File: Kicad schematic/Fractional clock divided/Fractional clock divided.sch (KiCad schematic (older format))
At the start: 51 parts, among them Q1 2N3904, Q2 2N3904, Q3 2N3904, Q4 2N3904, SW1 SPDT on-on, SW2 SPDT on-off-on, SW3 SPDT on-on, SW4 Rotary_Encoder_Switch, U1 TL074, U2 Teensy-LC

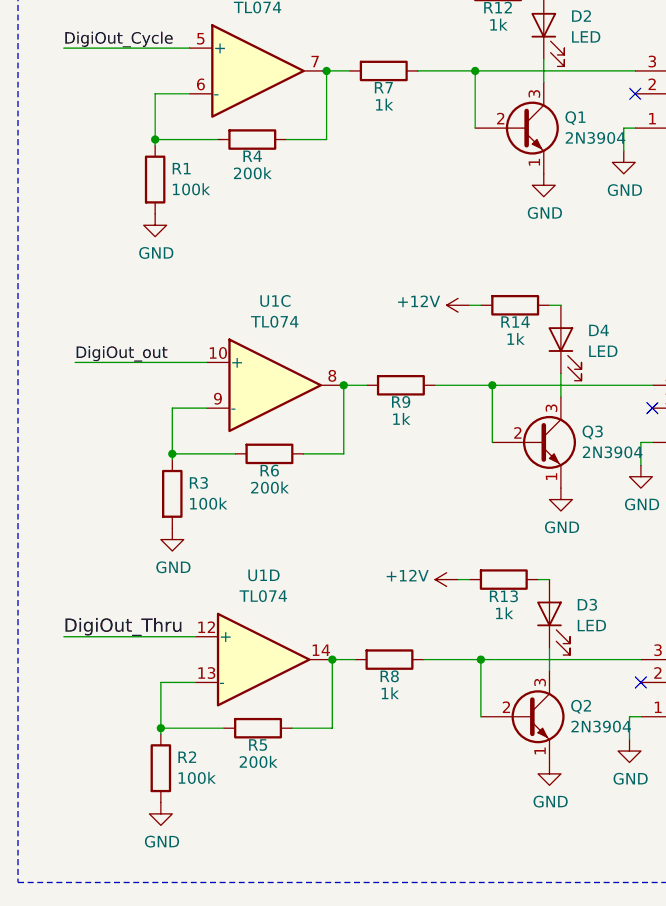
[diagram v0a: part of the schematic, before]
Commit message: Changed output voltages to 5V.
Changed all output voltages to 5V.
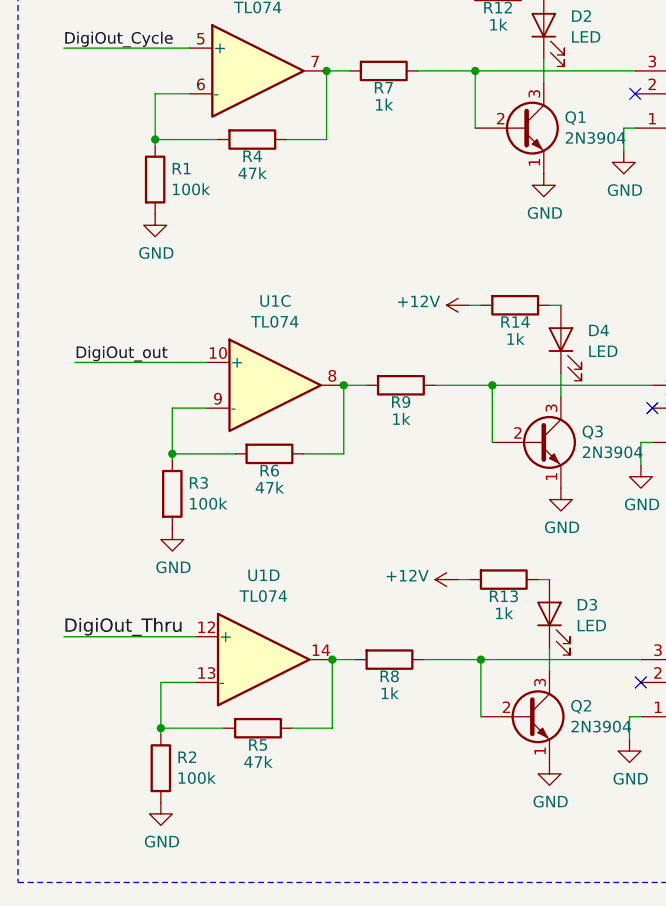
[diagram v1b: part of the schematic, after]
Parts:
- R4, R5, R6: value 200k -> 47k
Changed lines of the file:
@@
 EESchema Schematic File Version 4
+LIBS:Fractional clock divided-cache
 EELAYER 26 0
 EELAYER END
@@
 P 1725 3850
 F 0 "R4" V 1800 3850 50  0000 C CNN
-F 1 "200k" V 1875 3850 50  0000 C CNN
+F 1 "47k" V 1875 3850 50  0000 C CNN
 F 2 "" V 1655 3850 50  0001 C CNN
 F 3 "~" H 1725 3850 50  0001 C CNN
@@
 P 1800 5225
 F 0 "R6" V 1875 5225 50  0000 C CNN
-F 1 "200k" V 1950 5225 50  0000 C CNN
+F 1 "47k" V 1950 5225 50  0000 C CNN
 F 2 "" V 1730 5225 50  0001 C CNN
 F 3 "~" H 1800 5225 50  0001 C CNN
@@
 P 1750 6425
 F 0 "R5" V 1825 6425 50  0000 C CNN
-F 1 "200k" V 1900 6425 50  0000 C CNN
+F 1 "47k" V 1900 6425 50  0000 C CNN
 F 2 "" V 1680 6425 50  0001 C CNN
 F 3 "~" H 1750 6425 50  0001 C CNN

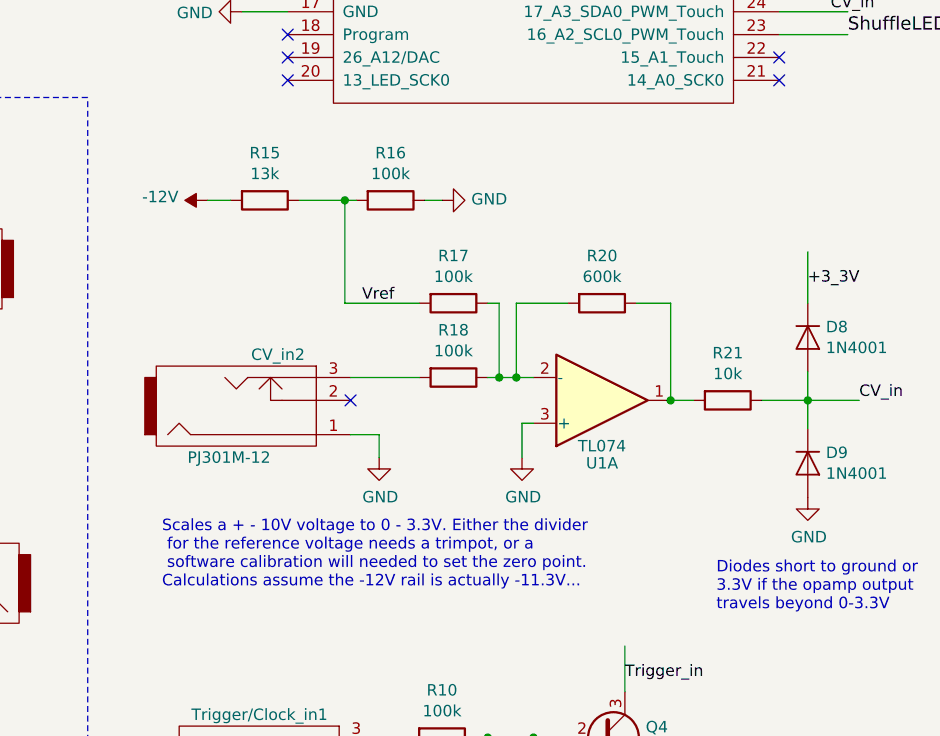
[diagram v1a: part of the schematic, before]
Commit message: Resistor substitution
Substituting resisitors to reflect what I have at-hand
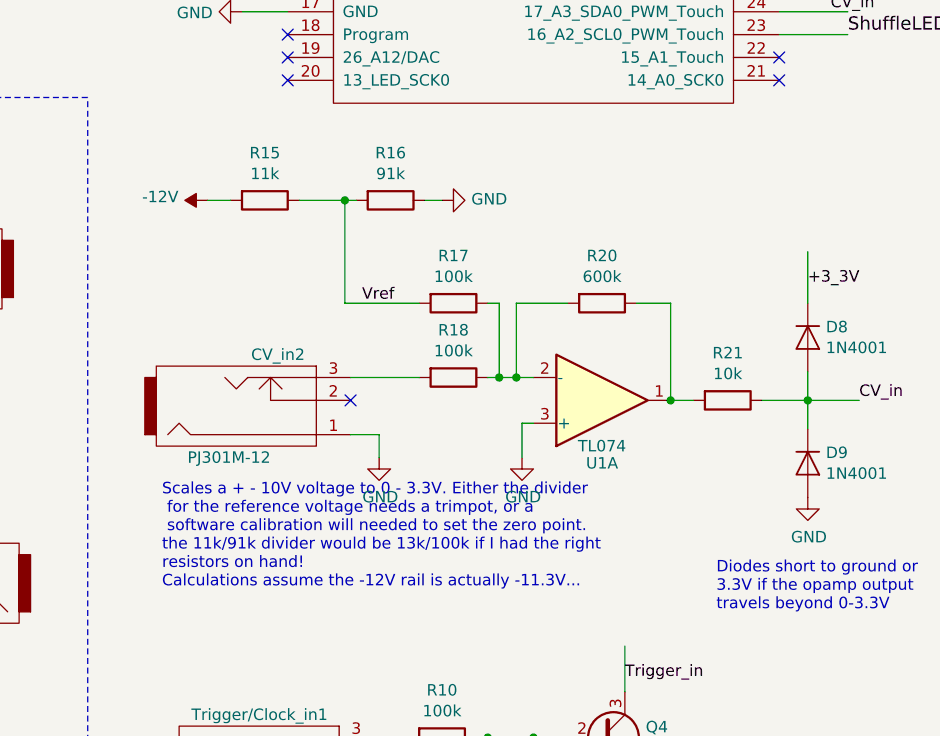
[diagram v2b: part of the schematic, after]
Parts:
- R15: value 13k -> 11k
- R16: value 100k -> 91k
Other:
- note added: "Scales a + - 10V voltage to 0 - 3.3V. Either the divider\n for the reference voltage needs a trimpot, or a\n software calibration will needed to set the zero point. \nthe 11k/91k divider would be 13k/100k if I had the right\nresistors on hand!\nCalculations assume the -12V rail is actually -11.3V..."
- note removed: "Scales a + - 10V voltage to 0 - 3.3V. Either the divider\n for the reference voltage needs a trimpot, or a\n software calibration will needed to set the zero point. \nCalculations assume the -12V rail is actually -11.3V..."
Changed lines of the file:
@@
 P 5400 3375
 F 0 "R15" V 5193 3375 50  0000 C CNN
-F 1 "13k" V 5284 3375 50  0000 C CNN
+F 1 "11k" V 5284 3375 50  0000 C CNN
 F 2 "" V 5330 3375 50  0001 C CNN
 F 3 "~" H 5400 3375 50  0001 C CNN
@@
 P 5950 3375
 F 0 "R16" V 5743 3375 50  0000 C CNN
-F 1 "100k" V 5834 3375 50  0000 C CNN
+F 1 "91k" V 5834 3375 50  0000 C CNN
 F 2 "" V 5880 3375 50  0001 C CNN
 F 3 "~" H 5950 3375 50  0001 C CNN
@@
 $EndComp
 Text Notes 4950 5075 0    50   ~ 0
-Scales a + - 10V voltage to 0 - 3.3V. Either the divider\n for the reference voltage needs a trimpot, or a\n software calibration will needed to set the zero point. \nCalculations assume the -12V rail is actually -11.3V...
+Scales a + - 10V voltage to 0 - 3.3V. Either the divider\n for the reference voltage needs a trimpot, or a\n software calibration will needed to set the zero point. \nthe 11k/91k divider would be 13k/100k if I had the right\nresistors on hand!\nCalculations assume the -12V rail is actually -11.3V...
 $Comp
 L Device:R R21

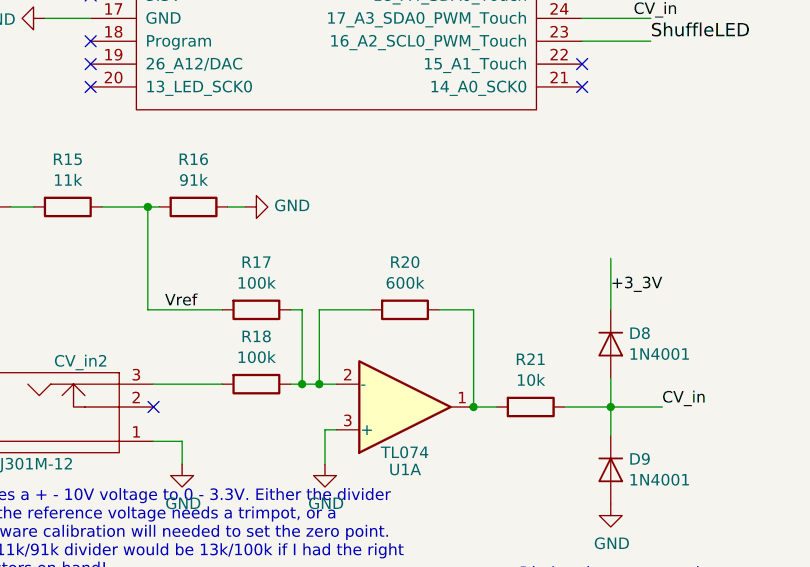
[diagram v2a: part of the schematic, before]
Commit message: Resistor substitutions
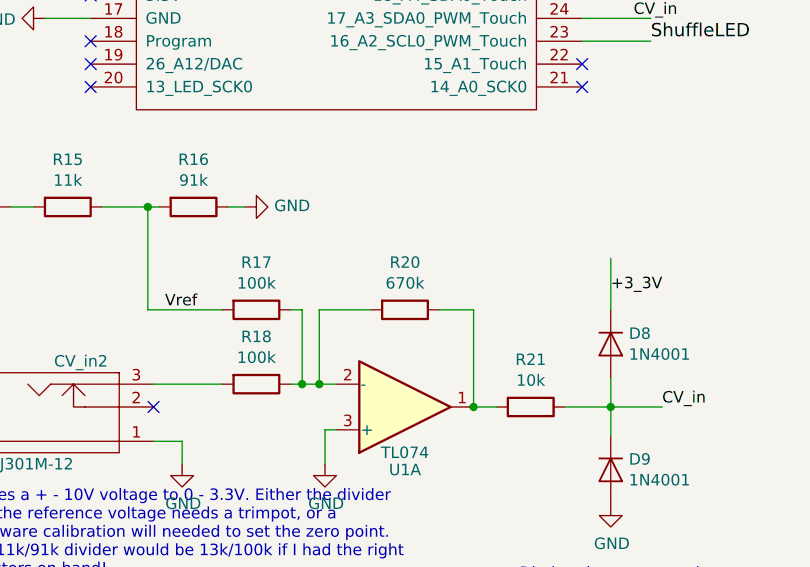
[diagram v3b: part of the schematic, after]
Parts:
- R20: value 600k -> 670k
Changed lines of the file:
@@
 P 6875 3825
 F 0 "R20" V 6668 3825 50  0000 C CNN
-F 1 "600k" V 6759 3825 50  0000 C CNN
+F 1 "670k" V 6759 3825 50  0000 C CNN
 F 2 "" V 6805 3825 50  0001 C CNN
 F 3 "~" H 6875 3825 50  0001 C CNN

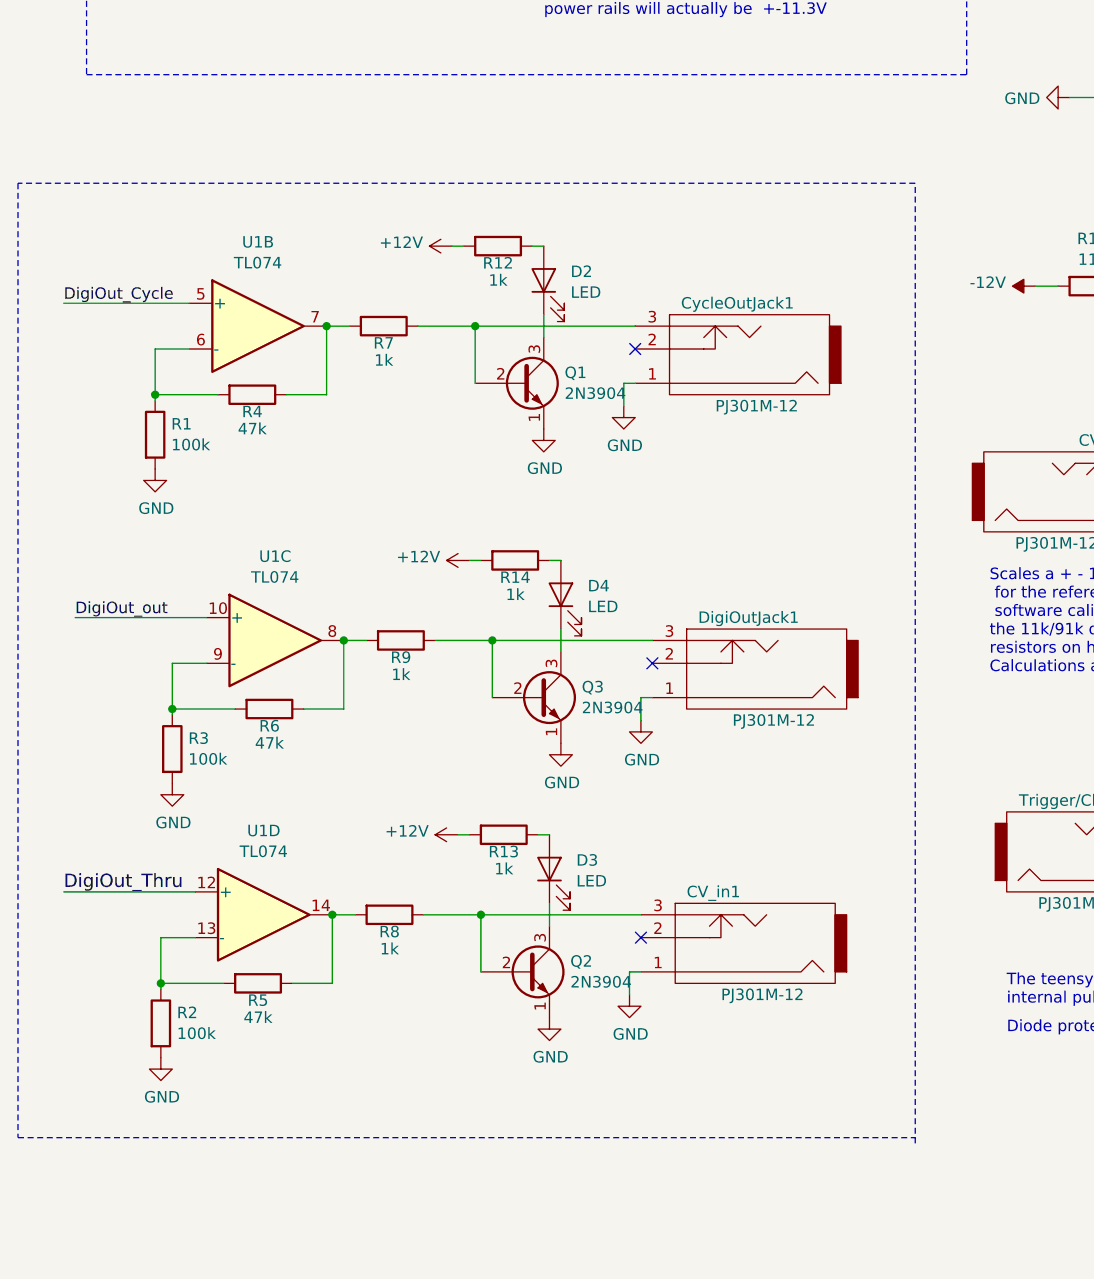
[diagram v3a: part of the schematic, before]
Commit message: Fixed LED output
Fixed a hardware bug with the output LEDs:  the current going into the transitior base was not being limited.
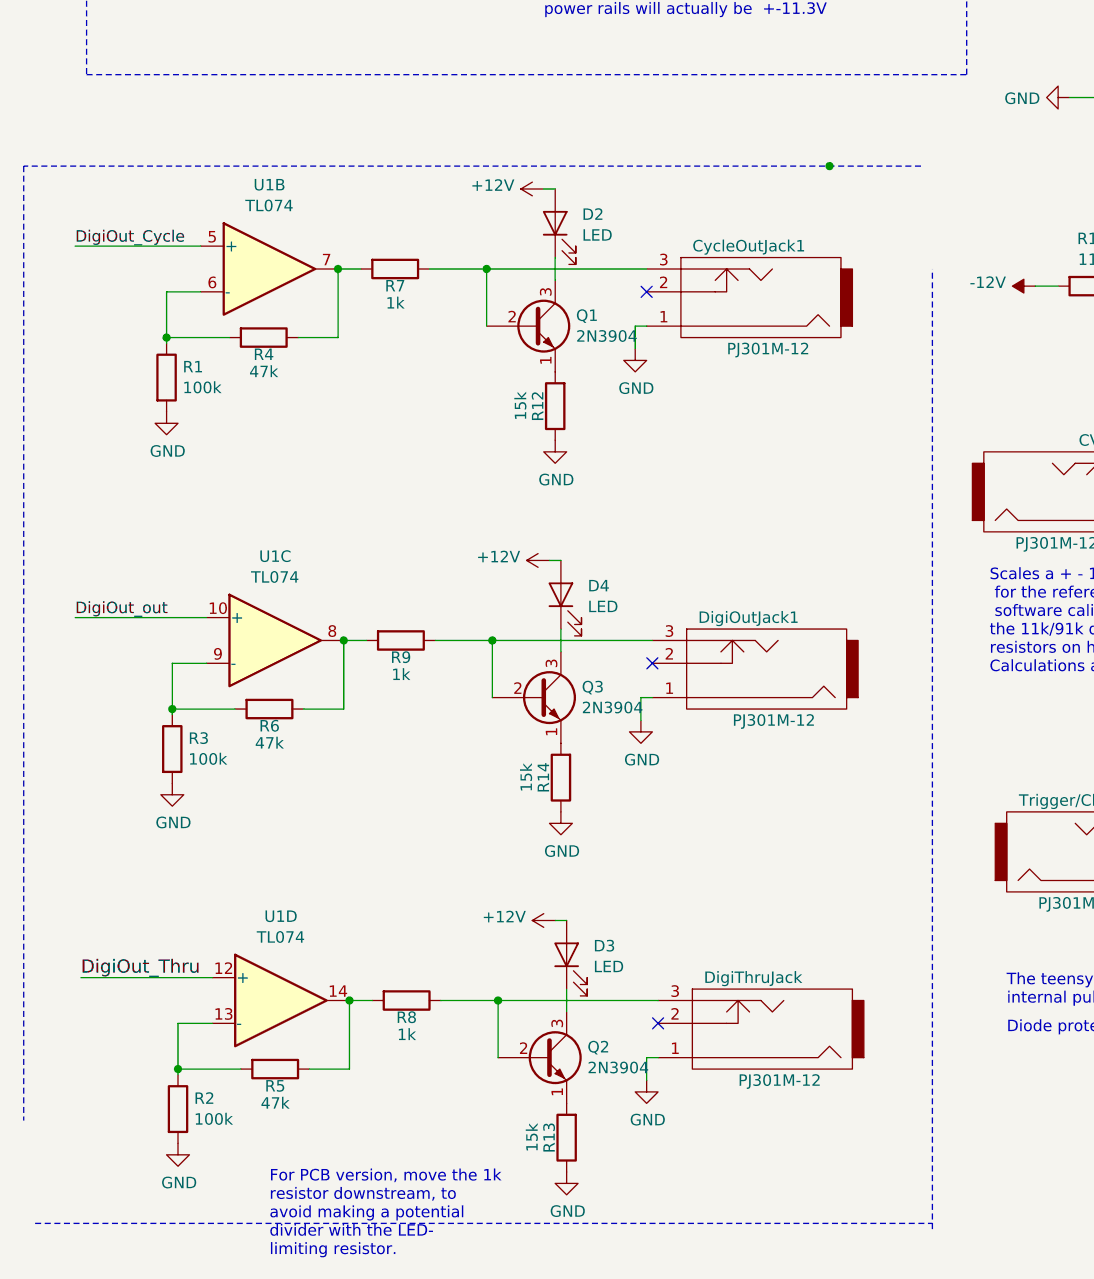
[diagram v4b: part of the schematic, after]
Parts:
- R12, R13, R14: value 1k -> 15k
- renumbered CV_in1 to DigiThruJack
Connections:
- wire segments 148 -> 145
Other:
- note added: "For PCB version, move the 1k\nresistor downstream, to \navoid making a potential \ndivider with the LED-\nlimiting resistor."
- moved on the sheet: CycleOutJack1, D2, D3, DigiThruJack, Q1, Q2, R1, R12, R13, R14, R2, R4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
